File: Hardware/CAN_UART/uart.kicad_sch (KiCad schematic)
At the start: 3 parts, among them IC1 ISO7721FQDWVRQ1

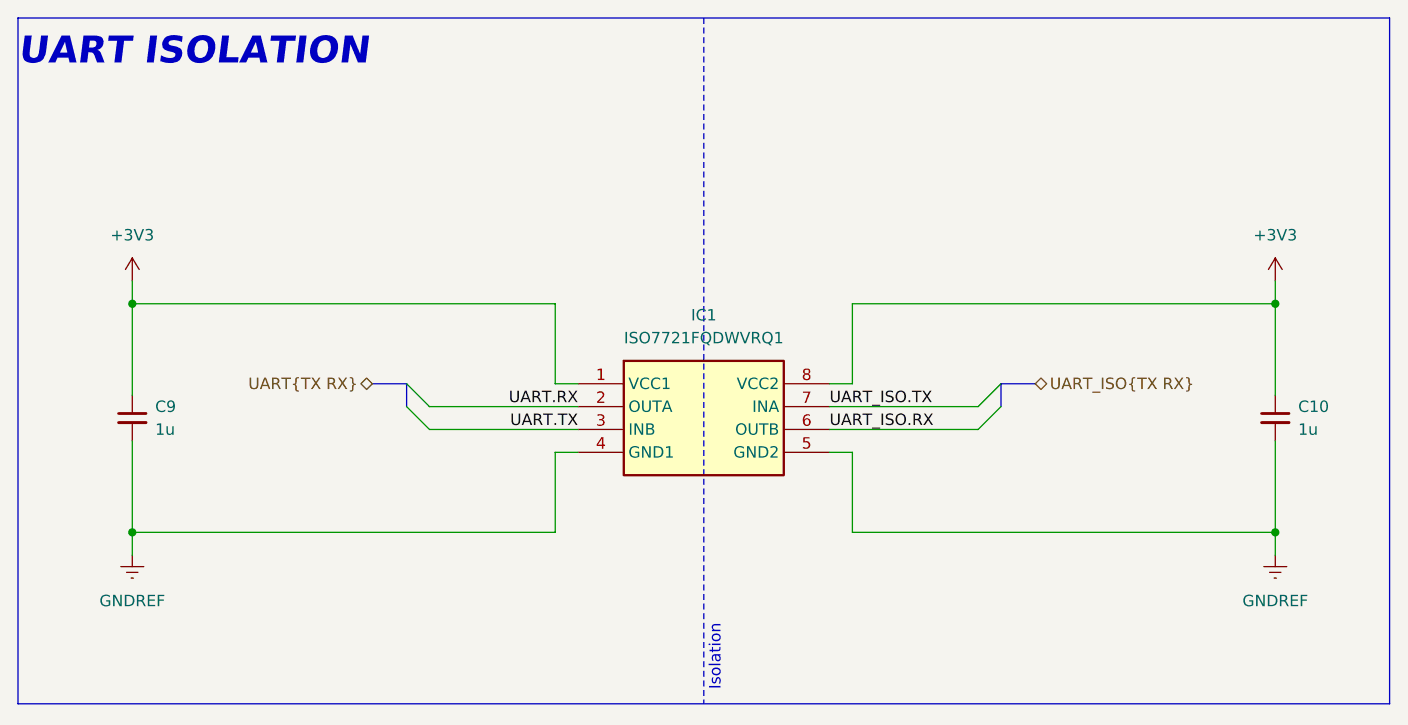
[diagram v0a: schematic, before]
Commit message: analog & can finished
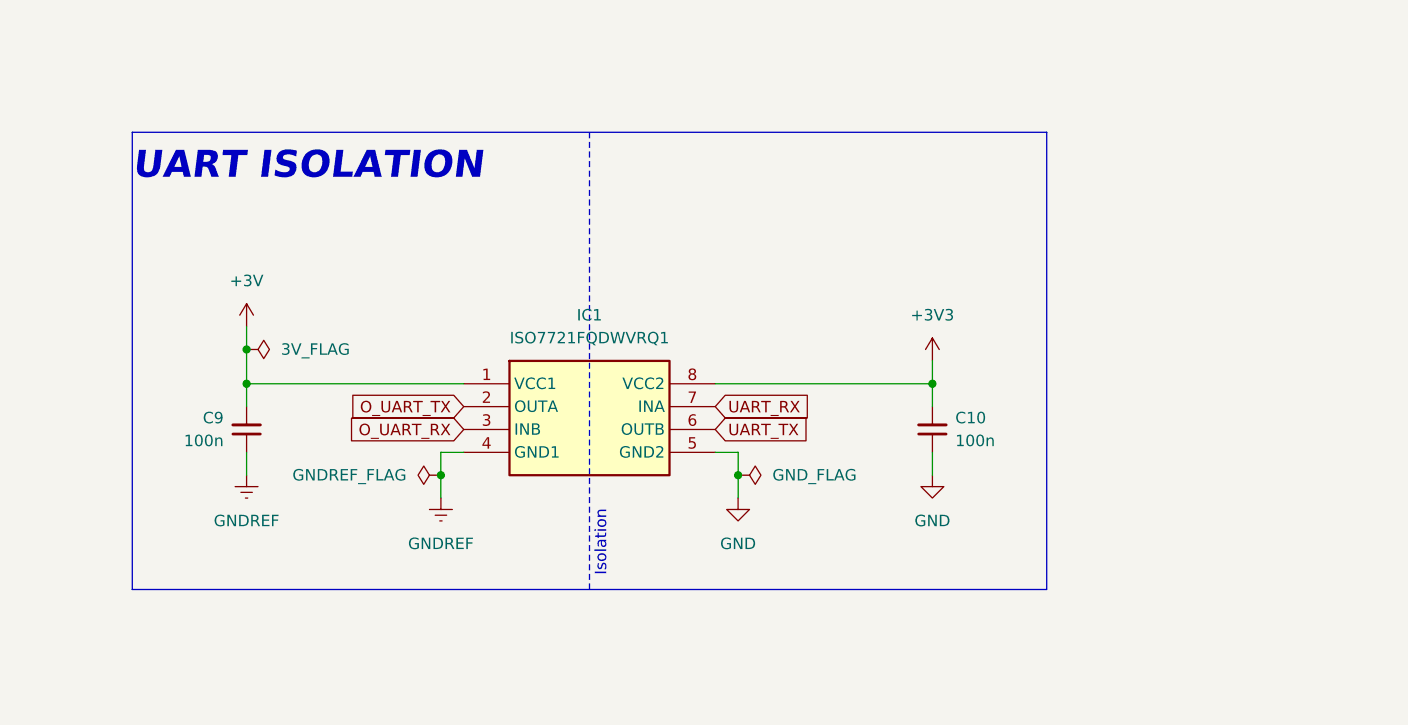
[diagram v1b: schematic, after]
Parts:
- C10, C9: value 1u -> 100n; footprint (none) -> Capacitor_SMD:C_0603_1608Metric_Pad1.08x0.95mm_HandSolder; Mouser Part Number (none) -> GRM033R6YA104ME14D; Mouser Price/Stock (none) -> https://www.mouser.pl/ProductDetail/Murata-Electronics/GRM0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
- IC1: footprint SOIC127P1150X280-8N -> PLC_STM:SOIC127P1150X280-8N
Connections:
- net +3V3: now also C10.2; no longer C10.1, C9.1, IC1.1 (VCC1)
- net GNDREF: now also C9.1; no longer C10.2, C9.2, IC1.5 (GND2)
- net UART.RX renamed O_UART_TX
- net UART.TX renamed O_UART_RX
- net UART_ISO.RX renamed UART_TX
- net UART_ISO.TX renamed UART_RX
- new net +3V: C9.2, IC1.1 (VCC1)
- new net GND: C10.1, IC1.5 (GND2)
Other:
- moved on the sheet: IC1
